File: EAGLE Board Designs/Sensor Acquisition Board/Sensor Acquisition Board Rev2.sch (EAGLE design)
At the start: 79 parts, among them J1 CONNECTOR-AVR-ISP__, J2 CONNECTOR-SENSOR_NF_S_RA_BLACK, J3 CONNECTOR-SENSOR_NF_S_RA_BLACK, J4 CONNECTOR-SENSOR_NF_S_RA_BLACK, J5 CONNECTOR-SENSOR_NF_S_RA_BLACK, J6 CONNECTOR-CAN_NF_S_RA_BLACK, U1 LM340, U10 OPAMP_1_CHANNEL_OPA991, U11 OPAMP_1_CHANNEL_OPA991, U12 OPAMP_1_CHANNEL_OPA991, U13 OPAMP_1_CHANNEL_OPA991, U2 ATMEGA328P-AU, U3 MCP2515, U4 MCP3204, U5 CAN_TRANSCIEVER_TCAN1051HQV-Q1, U6 MAX7400, U7 MAX7400, U8 MAX7400, U9 MAX7400, X1 CRYSTAL16MHZ, X2 CRYSTAL16MHZ

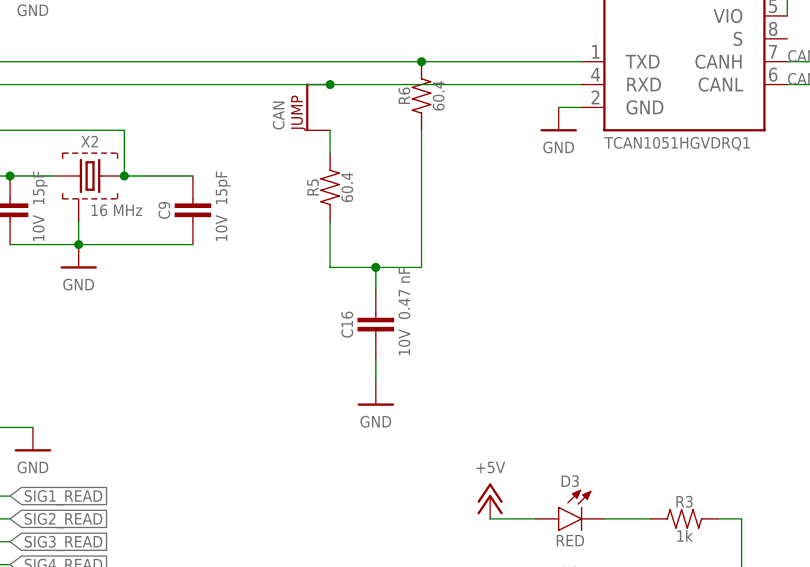
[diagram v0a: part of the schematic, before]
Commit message: Fixed technologies
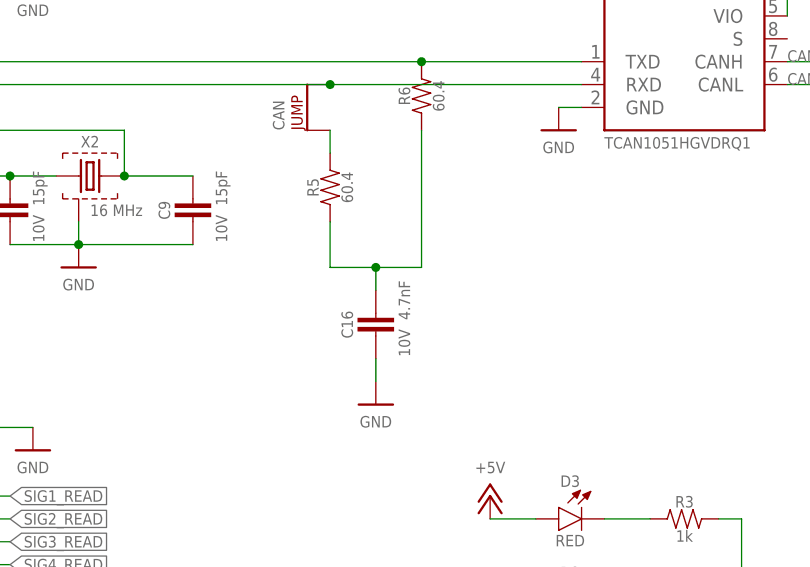
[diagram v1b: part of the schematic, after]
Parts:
- C16: value CAPACITOR_0603_10V_0.1UF -> CAPACITOR_0603_10V_4.7NF; device HyTechDevices:CAPACITOR_0603_10V_0.1UF -> HyTechDevices:CAPACITOR_0603_10V_4.7NF; CAPACITANCE 0.47 nF -> (none)
- R5, R6: value RESISTOR_0603_1K -> RESISTOR_0603_60.4; device HyTechDevices:RESISTOR_0603_1K -> HyTechDevices:RESISTOR_0603_60.4; RESISTANCE 60.4 -> (none)
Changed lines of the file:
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@@
 <grid distance="0.1" unitdist="inch" unit="inch" style="lines" multiple="1" display="no" altdistance="0.01" altunitdist="inch" altunit="inch"/>
 <layers>
-<layer number="1" name="Top" color="4" fill="1" visible="no" active="no"/>
-<layer number="2" name="Route2" color="1" fill="3" visible="no" active="no"/>
-<layer number="3" name="Route3" color="4" fill="3" visible="no" active="no"/>
-<layer number="4" name="Route4" color="1" fill="4" visible="no" active="no"/>
-<layer number="5" name="Route5" color="4" fill="4" visible="no" active="no"/>
-<layer number="6" name="Route6" color="1" fill="8" visible="no" active="no"/>
-<layer number="7" name="Route7" color="4" fill="8" visible="no" active="no"/>
-<layer number="8" name="Route8" color="1" fill="2" visible="no" active="no"/>
-<layer number="9" name="Route9" color="4" fill="2" visible="no" active="no"/>
-<layer number="10" name="Route10" color="1" fill="7" visible="no" active="no"/>
-<layer number="11" name="Route11" color="4" fill="7" visible="no" active="no"/>
-<layer number="12" name="Route12" color="1" fill="5" visible="no" active="no"/>
-<layer number="13" name="Route13" color="4" fill="5" visible="no" active="no"/>
-<layer number="14" name="Route14" color="1" fill="6" visible="no" active="no"/>
-<layer number="15" name="Route15" color="4" fill="6" visible="no" active="no"/>
-<layer number="16" name="Bottom" color="1" fill="1" visible="no" active="no"/>
-<layer number="17" name="Pads" color="2" fill="1" visible="no" active="no"/>
-<layer number="18" name="Vias" color="2" fill="1" visible="no" active="no"/>
-<layer number="19" name="Unrouted" color="6" fill="1" visible="no" active="no"/>
-<layer number="20" name="Dimension" color="24" fill="1" visible="no" active="no"/>
-<layer number="21" name="tPlace" color="7" fill="1" visible="no" active="no"/>
-<layer number="22" name="bPlace" color="7" fill="1" visible="no" active="no"/>
-<layer number="23" name="tOrigins" color="15" fill="1" visible="no" active="no"/>
-<layer number="24" name="bOrigins" color="15" fill="1" visible="no" active="no"/>
-<layer number="25" name="tNames" color="7" fill="1" visible="no" active="no"/>
-<layer number="26" name="bNames" color="7" fill="1" visible="no" active="no"/>
-<layer number="27" name="tValues" color="7" fill="1" visible="no" active="no"/>
-<layer number="28" name="bValues" color="7" fill="1" visible="no" active="no"/>
+<layer number="1" name="Top" color="4" fill="1" visible="yes" active="no"/>
+<layer number="2" name="Route2" color="1" fill="3" visible="yes" active="no"/>
+<layer number="3" name="Route3" color="4" fill="3" visible="yes" active="no"/>
+<layer number="4" name="Route4" color="1" fill="4" visible="yes" active="no"/>
+<layer number="5" name="Route5" color="4" fill="4" visible="yes" active="no"/>
+<layer number="6" name="Route6" color="1" fill="8" visible="yes" active="no"/>
+<layer number="7" name="Route7" color="4" fill="8" visible="yes" active="no"/>
+<layer number="8" name="Route8" color="1" fill="2" visible="yes" active="no"/>
+<layer number="9" name="Route9" color="4" fill="2" visible="yes" active="no"/>
+<layer number="10" name="Route10" color="1" fill="7" visible="yes" active="no"/>
+<layer number="11" name="Route11" color="4" fill="7" visible="yes" active="no"/>
+<layer number="12" name="Route12" color="1" fill="5" visible="yes" active="no"/>
+<layer number="13" name="Route13" color="4" fill="5" visible="yes" active="no"/>
+<layer number="14" name="Route14" color="1" fill="6" visible="yes" active="no"/>
+<layer number="15" name="Route15" color="4" fill="6" visible="yes" active="no"/>
+<layer number="16" name="Bottom" color="1" fill="1" visible="yes" active="no"/>
+<layer number="17" name="Pads" color="2" fill="1" visible="yes" active="no"/>
+<layer number="18" name="Vias" color="2" fill="1" visible="yes" active="no"/>
+<layer number="19" name="Unrouted" color="6" fill="1" visible="yes" active="no"/>
+<layer number="20" name="Dimension" color="24" fill="1" visible="yes" active="no"/>
+<layer number="21" name="tPlace" color="7" fill="1" visible="yes" active="no"/>
+<layer number="22" name="bPlace" color="7" fill="1" visible="yes" active="no"/>
+<layer number="23" name="tOrigins" color="15" fill="1" visible="yes" active="no"/>
+<layer number="24" name="bOrigins" color="15" fill="1" visible="yes" active="no"/>
+<layer number="25" name="tNames" color="7" fill="1" visible="yes" active="no"/>
+<layer number="26" name="bNames" color="7" fill="1" visible="yes" active="no"/>
+<layer number="27" name="tValues" color="7" fill="1" visible="yes" active="no"/>
+<layer number="28" name="bValues" color="7" fill="1" visible="yes" active="no"/>
 <layer number="29" name="tStop" color="7" fill="3" visible="no" active="no"/>
 <layer number="30" name="bStop" color="7" fill="6" visible="no" active="no"/>
@@
 <layer number="35" name="tGlue" color="7" fill="4" visible="no" active="no"/>
 <layer number="36" name="bGlue" color="7" fill="5" visible="no" active="no"/>
-<layer number="37" name="tTest" color="7" fill="1" visible="no" active="no"/>
-<layer number="38" name="bTest" color="7" fill="1" visible="no" active="no"/>
+<layer number="37" name="tTest" color="7" fill="1" visible="yes" active="no"/>
+<layer number="38" name="bTest" color="7" fill="1" visible="yes" active="no"/>
 <layer number="39" name="tKeepout" color="4" fill="11" visible="no" active="no"/>
 <layer number="40" name="bKeepout" color="1" fill="11" visible="no" active="no"/>
@@
 <layer number="44" name="Drills" color="7" fill="1" visible="no" active="no"/>
 <layer number="45" name="Holes" color="7" fill="1" visible="no" active="no"/>
-<layer number="46" name="Milling" color="3" fill="1" visible="no" active="no"/>
-<layer number="47" name="Measures" color="7" fill="1" visible="no" active="no"/>
-<layer number="48" name="Document" color="7" fill="1" visible="no" active="no"/>
-<layer number="49" name="Reference" color="7" fill="1" visible="no" active="no"/>
-<layer number="50" name="dxf" color="7" fill="1" visible="no" active="no"/>
-<layer number="51" name="tDocu" color="7" fill="1" visible="no" active="no"/>
-<layer number="52" name="bDocu" color="7" fill="1" visible="no" active="no"/>
-<layer number="53" name="tGND_GNDA" color="7" fill="9" visible="no" active="no"/>
-<layer number="54" name="bGND_GNDA" color="1" fill="9" visible="no" active="no"/>
-<layer number="56" name="wert" color="7" fill="1" visible="no" active="no"/>
-<layer number="57" name="tCAD" color="7" fill="1" visible="no" active="no"/>
-<layer number="59" name="tCarbon" color="7" fill="1" visible="no" active="no"/>
-<layer number="60" name="bCarbon" color="7" fill="1" visible="no" active="no"/>
+<layer number="46" name="Milling" color="3" fill="1" visible="yes" active="no"/>
+<layer number="47" name="Measures" color="7" fill="1" visible="yes" active="no"/>
+<layer number="48" name="Document" color="7" fill="1" visible="yes" active="no"/>
+<layer number="49" name="Reference" color="7" fill="1" visible="yes" active="no"/>
+<layer number="50" name="dxf" color="7" fill="1" visible="yes" active="no"/>
+<layer number="51" name="tDocu" color="7" fill="1" visible="yes" active="no"/>
+<layer number="52" name="bDocu" color="7" fill="1" visible="yes" active="no"/>
+<layer number="53" name="tGND_GNDA" color="7" fill="9" visible="yes" active="no"/>
+<layer number="54" name="bGND_GNDA" color="1" fill="9" visible="yes" active="no"/>
+<layer number="56" name="wert" color="7" fill="1" visible="yes" active="no"/>
+<layer number="57" name="tCAD" color="7" fill="1" visible="yes" active="no"/>
+<layer number="59" name="tCarbon" color="7" fill="1" visible="yes" active="no"/>
+<layer number="60" name="bCarbon" color="7" fill="1" visible="yes" active="no"/>
 <layer number="88" name="SimResults" color="9" fill="1" visible="yes" active="yes"/>
 <layer number="89" name="SimProbes" color="9" fill="1" visible="yes" active="yes"/>
@@
 <part name="P+8" library="HyTechSupplies" deviceset="+5V" device=""/>
 <part name="C14" library="HyTechDevices" deviceset="CAPACITOR_?_*" device="0603" technology="10V_1UF"/>
-<part name="R5" library="HyTechDevices" deviceset="RESISTOR_?_*" device="0603" technology="1K">
-<attribute name="RESISTANCE" value="60.4"/>
-</part>
-<part name="R6" library="HyTechDevices" deviceset="RESISTOR_?_*" device="0603" technology="1K">
-<attribute name="RESISTANCE" value="60.4"/>
-</part>
+<part name="R5" library="HyTechDevices" deviceset="RESISTOR_?_*" device="0603" technology="60.4" value="RESISTOR_0603_60.4"/>
+<part name="R6" library="HyTechDevices" deviceset="RESISTOR_?_*" device="0603" technology="60.4" value="RESISTOR_0603_60.4"/>
 <part name="CAN" library="HyTechDevices" deviceset="JUMPER_?_*" device="1X02"/>
-<part name="C16" library="HyTechDevices" deviceset="CAPACITOR_?_*" device="0603" technology="10V_0.1UF">
-<attribute name="CAPACITANCE" value="0.47 nF"/>
-</part>
+<part name="C16" library="HyTechDevices" deviceset="CAPACITOR_?_*" device="0603" technology="10V_4.7NF" value="CAPACITOR_0603_10V_4.7NF"/>
 <part name="GND12" library="HyTechSupplies" deviceset="GND" device=""/>
 <part name="U$7" library="HyTechFrames" deviceset="FRAME_B" device=""/>
